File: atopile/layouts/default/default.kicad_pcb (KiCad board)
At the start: 2 copper layers, 78 x 60 mm, 86 parts

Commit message: Add schematic PDF export and name remaining nets
- scripts/export_schematic.py: builds a hierarchical KiCad schematic
  from atopile's outputs (PCB netlist, BOM values, per-part symbols),
  one sheet per subsystem with a net label on every pin, plots it with
  kicad-cli and verifies the schematic netlist matches the atopile
  netlist net-for-net
- schematic/: generated KiCad 10 schematic + solartron_7075_usb.pdf
- Name previously auto-named nets in the .ato source (XIN, XTAL_OUT,
  VREG_AVDD, BOOTSEL_SW, LDO_FB, STATUS_LED, LED anodes, shift-register
  chain links, SAMPLE_CONTACT_GATE)
- README: schematic section and converter circle-syntax note

Co-Authored-By: Claude Opus 5.5 <noreply@anthropic.com>
Claude-Session: https://claude.ai/code/session_01NqBEt2iCuw3VMJkgzgPtpr
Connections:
- net 37 renamed STATUS_LED
- net DS renamed SI_CHAIN_1
- net G renamed SAMPLE_CONTACT_GATE
- net anode renamed LED_ISO_A
- net anode-1 renamed LED_PWR_A
- net anode-2 renamed LED_STATUS_A
- net crystal_load[0]-power-hv renamed XIN
- net crystal_load[1]-power-hv renamed XTAL_OUT
- net hv renamed LDO_FB
- net input renamed BOOTSEL_SW
- net serial_in-DS renamed SO_CHAIN_1
- net shift_in[2]-q7-DS renamed SI_CHAIN_2
- net shift_in[3]-q7-DS renamed SI_CHAIN_3
- net shift_in[4]-q7-DS renamed SI_CHAIN_4
- net vreg_avdd_c-power-hv renamed VREG_AVDD
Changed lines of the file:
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@@
 	(net 30 "SKB50_RANGE_CMD_4")
 	(net 31 "SKB09_D4_1")
-	(net 32 "anode")
-	(net 33 "hv")
+	(net 32 "LED_ISO_A")
+	(net 33 "LDO_FB")
 	(net 34 "DNC")
-	(net 35 "input")
+	(net 35 "BOOTSEL_SW")
 	(net 36 "QSPI_SS")
-	(net 37 "crystal_load[0]-power-hv")
-	(net 38 "crystal_load[1]-power-hv")
+	(net 37 "XIN")
+	(net 38 "XTAL_OUT")
 	(net 39 "GND")
 	(net 40 "10")
@@
 	(net 56 "35")
 	(net 57 "36")
-	(net 58 "37")
+	(net 58 "STATUS_LED")
 	(net 59 "+1V1")
 	(net 60 "4")
@@
 	(net 63 "42")
 	(net 64 "43")
-	(net 65 "vreg_avdd_c-power-hv")
+	(net 65 "VREG_AVDD")
 	(net 66 "VREG_LX")
 	(net 67 "5")
@@
 	(net 93 "opto_sck-AN")
 	(net 94 "SCK")
-	(net 95 "anode-1")
-	(net 96 "DS")
+	(net 95 "LED_PWR_A")
+	(net 96 "SI_CHAIN_1")
 	(net 97 "SKB08_D4_2")
 	(net 98 "SKB07_D4_4")
@@
 	(net 108 "SKB13_D3_1")
 	(net 109 "shift_in[1]-q7_n-7")
-	(net 110 "shift_in[3]-q7-DS")
+	(net 110 "SI_CHAIN_3")
 	(net 111 "SKB23_D0_4")
 	(net 112 "SKB22_D0_8")
@@
 	(net 114 "SKB20_D1_2")
 	(net 115 "shift_in[2]-q7_n-7")
-	(net 116 "shift_in[2]-q7-DS")
+	(net 116 "SI_CHAIN_2")
 	(net 117 "SKB29_FUNC_OUT_B")
 	(net 118 "SKB28_FUNC_OUT_A")
@@
 	(net 123 "SKB35_DATA_CAN_CHANGE")
 	(net 124 "shift_in[4]-q7_n-7")
-	(net 125 "shift_in[4]-q7-DS")
-	(net 126 "G")
+	(net 125 "SI_CHAIN_4")
+	(net 126 "SAMPLE_CONTACT_GATE")
 	(net 127 "OE_N_ISO")
 	(net 128 "MOSI_ISO")
-	(net 129 "serial_in-DS")
+	(net 129 "SO_CHAIN_1")
 	(net 130 "q[5]-5")
 	(net 131 "6")
 	(net 132 "q[7]-7")
 	(net 133 "Q7S")
-	(net 134 "anode-2")
+	(net 134 "LED_STATUS_A")
 	(net 135 "SWO")
 	(net 136 "DATA_P")
@@
 			(size 0.36 0.61)
 			(layers "F.Cu" "F.Paste" "F.Mask")
-			(net 33 "hv")
+			(net 33 "LDO_FB")
 		)
 		(pad "3" smd oval
@@
 			(size 0.2 0.88)
 			(layers "F.Cu" "F.Paste" "F.Mask")
-			(net 65 "vreg_avdd_c-power-hv")
+			(net 65 "VREG_AVDD")
 		)
 		(pad "45" smd rect
@@
 			(size 0.88 0.2)
 			(layers "F.Cu" "F.Paste" "F.Mask")
-			(net 58 "37")
+			(net 58 "STATUS_LED")
 		)
 		(pad "36" smd rect
@@
 			(size 0.2 0.88)
 			(layers "F.Cu" "F.Paste" "F.Mask")
-			(net 37 "crystal_load[0]-power-hv")
+			(net 37 "XIN")
 		)
 		(pad "20" smd rect
@@
 			(size 1.4 1.2)
 			(layers "F.Cu" "F.Paste" "F.Mask")
-			(net 37 "crystal_load[0]-power-hv")
+			(net 37 "XIN")
 		)
 		(pad "2" smd rect
@@
 			(size 1.4 1.2)
 			(layers "F.Cu" "F.Paste" "F.Mask")
-			(net 38 "crystal_load[1]-power-hv")
+			(net 38 "XTAL_OUT")
 		)
 		(pad "4" smd rect
@@
 			(size 1.05 0.7)
 			(layers "F.Cu" "F.Paste" "F.Mask")
-			(net 35 "input")
+			(net 35 "BOOTSEL_SW")
 		)
 		(pad "2" smd rect
@@
 			(size 1.05 0.7)
 			(layers "F.Cu" "F.Paste" "F.Mask")
-			(net 35 "input")
+			(net 35 "BOOTSEL_SW")
 		)
 		(pad "3" smd rect
@@
 			(size 0.8 0.8)
 			(layers "F.Cu" "F.Paste" "F.Mask")
-			(net 95 "anode-1")
+			(net 95 "LED_PWR_A")
 		)
 		(pad "1" smd rect
@@
 			(size 0.8 0.8)
 			(layers "F.Cu" "F.Paste" "F.Mask")
-			(net 134 "anode-2")
+			(net 134 "LED_STATUS_A")
 		)
 		(pad "2" smd rect
@@
 			(size 0.8 0.8)
 			(layers "F.Cu" "F.Paste" "F.Mask")
-			(net 32 "anode")
+			(net 32 "LED_ISO_A")
 		)
 		(pad "1" smd rect
@@
 			(size 0.6 1.97)
 			(layers "F.Cu" "F.Paste" "F.Mask")
-			(net 96 "DS")
+			(net 96 "SI_CHAIN_1")
 		)
 		(pad "9" smd oval
@@
 			(size 0.6 1.97)
 			(layers "F.Cu" "F.Paste" "F.Mask")
-			(net 116 "shift_in[2]-q7-DS")
+			(net 116 "SI_CHAIN_2")
 		)
 		(pad "9" smd oval
@@
 			(size 0.6 1.97)
 			(layers "F.Cu" "F.Paste" "F.Mask")
-			(net 96 "DS")
+			(net 96 "SI_CHAIN_1")
 		)
 		(embedded_fonts no)
@@
 			(size 0.6 1.97)
 			(layers "F.Cu" "F.Paste" "F.Mask")
-			(net 110 "shift_in[3]-q7-DS")
+			(net 110 "SI_CHAIN_3")
 		)
 		(pad "9" smd oval
@@
 			(size 0.6 1.97)
 			(layers "F.Cu" "F.Paste" "F.Mask")
-			(net 116 "shift_in[2]-q7-DS")
+			(net 116 "SI_CHAIN_2")
 		)
 		(embedded_fonts no)
@@
 			(size 0.6 1.97)
 			(layers "F.Cu" "F.Paste" "F.Mask")
-			(net 125 "shift_in[4]-q7-DS")
+			(net 125 "SI_CHAIN_4")
 		)
 		(pad "9" smd oval
@@
 			(size 0.6 1.97)
 			(layers "F.Cu" "F.Paste" "F.Mask")
-			(net 110 "shift_in[3]-q7-DS")
+			(net 110 "SI_CHAIN_3")
 		)
 		(embedded_fonts no)
@@
 			(size 0.6 1.97)
 			(layers "F.Cu" "F.Paste" "F.Mask")
-			(net 125 "shift_in[4]-q7-DS")
+			(net 125 "SI_CHAIN_4")
 		)
 		(embedded_fonts no)
@@
 			(size 0.6 1.97)
 			(layers "F.Cu" "F.Paste" "F.Mask")
-			(net 126 "G")
+			(net 126 "SAMPLE_CONTACT_GATE")
 		)
 		(pad "2" smd oval
@@
 			(size 0.6 1.97)
 			(layers "F.Cu" "F.Paste" "F.Mask")
-			(net 129 "serial_in-DS")
+			(net 129 "SO_CHAIN_1")
 		)
 		(embedded_fonts no)
@@
 			(size 0.6 1.97)
 			(layers "F.Cu" "F.Paste" "F.Mask")
-			(net 129 "serial_in-DS")
+			(net 129 "SO_CHAIN_1")
 		)
 		(pad "13" smd oval
@@
 			(size 1 0.65)
 			(layers "F.Cu" "F.Paste" "F.Mask")
-			(net 126 "G")
+			(net 126 "SAMPLE_CONTACT_GATE")
 		)
 		(pad "2" smd rect
@@
 			(size 0.57 0.54)
 			(layers "F.Cu" "F.Paste" "F.Mask")
-			(net 32 "anode")
+			(net 32 "LED_ISO_A")
 		)
 		(pad "1" smd rect
@@
 			(size 0.57 0.54)
 			(layers "F.Cu" "F.Paste" "F.Mask")
-			(net 33 "hv")
+			(net 33 "LDO_FB")
 		)
 		(pad "1" smd rect
@@
 			(size 0.57 0.54)
 			(layers "F.Cu" "F.Paste" "F.Mask")
-			(net 126 "G")
+			(net 126 "SAMPLE_CONTACT_GATE")
 		)
 		(embedded_fonts no)
@@
 			(size 0.57 0.54)
 			(layers "F.Cu" "F.Paste" "F.Mask")
-			(net 33 "hv")
+			(net 33 "LDO_FB")
 		)
 		(embedded_fonts no)
@@
 			(size 0.57 0.54)
 			(layers "F.Cu" "F.Paste" "F.Mask")
-			(net 35 "input")
+			(net 35 "BOOTSEL_SW")
 		)
 		(pad "1" smd rect
@@
 			(size 0.57 0.54)
 			(layers "F.Cu" "F.Paste" "F.Mask")
-			(net 38 "crystal_load[1]-power-hv")
+			(net 38 "XTAL_OUT")
 		)
 		(pad "1" smd rect
@@
 			(size 0.5 0.54)
 			(layers "F.Cu" "F.Paste" "F.Mask")
-			(net 37 "crystal_load[0]-power-hv")
+			(net 37 "XIN")
 		)
 		(embedded_fonts no)
@@
 			(size 0.5 0.54)
 			(layers "F.Cu" "F.Paste" "F.Mask")
-			(net 38 "crystal_load[1]-power-hv")
+			(net 38 "XTAL_OUT")
 		)
 		(embedded_fonts no)
@@
 			(size 0.5 0.54)
 			(layers "F.Cu" "F.Paste" "F.Mask")
-			(net 65 "vreg_avdd_c-power-hv")
+			(net 65 "VREG_AVDD")
 		)
 		(embedded_fonts no)
@@
 			(size 0.57 0.54)
 			(layers "F.Cu" "F.Paste" "F.Mask")
-			(net 65 "vreg_avdd_c-power-hv")
+			(net 65 "VREG_AVDD")
 		)
 		(pad "1" smd rect
@@
 			(size 0.57 0.54)
 			(layers "F.Cu" "F.Paste" "F.Mask")
-			(net 95 "anode-1")
+			(net 95 "LED_PWR_A")
 		)
 		(pad "1" smd rect
@@
 			(size 0.57 0.54)
 			(layers "F.Cu" "F.Paste" "F.Mask")
-			(net 134 "anode-2")
+			(net 134 "LED_STATUS_A")
 		)
 		(pad "1" smd rect
@@
 			(size 0.57 0.54)
 			(layers "F.Cu" "F.Paste" "F.Mask")
-			(net 58 "37")
+			(net 58 "STATUS_LED")
 		)
 		(embedded_fonts no)

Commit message: atopile: gerbers, 1:1 prints and 3D renders of the PCB
- scripts/export_pcb.py: DRC with zone refill, gerbers + Excellon drill
  (zipped, named _UNROUTED_ while DRC reports unrouted connections),
  3-page 1:1 A4 prints with title block, and 3D renders, all from a
  temporary copy of the atopile layout
- layouts/default/default.kicad_pro: JLCPCB 2-layer design rules
- place_components.py: move the pre-routed TLV75901 block (parts,
  tracks, vias) rigidly; pours to the barrier edge; DC-DC and R10 moved
  clear of the board edge; zone polygons without uuid (KiCad 10)
- check_layout.py: pad-to-pad check inside pre-routed library blocks
- Fix EasyEDA 3D model offsets for IB0505LS (y), USB-B (z) and DD-50 (z)
- README: PCB outputs section, DRC status, stack-up and tool notes

The board is still unrouted; the gerbers are for fit checks only.

Co-Authored-By: Claude Opus 5.5 <noreply@anthropic.com>
Claude-Session: https://claude.ai/code/session_01NqBEt2iCuw3VMJkgzgPtpr
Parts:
- moved C4 4.64 mm to (-10.3, -23.2), turned to 180 degrees
- moved R3 4.54 mm to (-13.8, -23.2)
- moved C5 4.46 mm to (-13.5, -26.7), turned to 0 degrees
- moved R2 3.17 mm to (-14.2, -25.0), turned to -90 degrees
- moved R10 1.90 mm to (-29.6, 3.80)
- moved U2 0.60 mm to (-33.4, 1.27)

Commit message: atopile: pin-swap the shift registers to untangle the DD-50 routing
- scripts/pin_swap.py: treats all 74HCT165 inputs, all 74HCT595 outputs
  and both chain orders as interchangeable, minimises ratsnest length +
  crossings (seeded simulated annealing) and regenerates the pin-map
  block in main.ato and the firmware bit-map tables in README.md
- DVM-side ratsnest: 1544 mm / 839 crossings -> 860 mm / 154 crossings;
  165 chain now follows the physical row (124 mm -> 56 mm)
- place_components.py: fixed register slots (the old centroid sort was
  not idempotent once the DD-50 sat on B.Cu and reversed the row)
- schematic, ERC and fab outputs regenerated; no parts moved

Co-Authored-By: Claude Opus 5.5 <noreply@anthropic.com>
Claude-Session: https://claude.ai/code/session_01NqBEt2iCuw3VMJkgzgPtpr
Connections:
- U12 pad 11: SKB08_D4_2 -> +5V_ISO
- U12 pad 12: SKB07_D4_4 -> +5V_ISO
- U12 pad 13: SKB06_D4_8 -> SKB32_RANGE_OUT_1
- U12 pad 14: SKB05_D5_1 -> SKB15_D2_4
- U12 pad 3: SKB04_D5_2 -> SKB17_D2_1
- U12 pad 4: SKB03_D5_4 -> SKB16_D2_2
- U12 pad 5: SKB02_D5_8 -> SKB33_PRINT_PULSE
- U12 pad 6: SKB01_D6_1 -> GND_ISO
- U13 pad 10: SI_CHAIN_2 -> GND_ISO
- U13 pad 11: SKB16_D2_2 -> SKB34_PRINT_LEVEL
- U13 pad 12: SKB15_D2_4 -> SKB01_D6_1
- U13 pad 13: SKB14_D2_8 -> SKB35_DATA_CAN_CHANGE
- U13 pad 14: SKB13_D3_1 -> SKB18_D1_8
- U13 pad 3: SKB12_D3_2 -> SKB03_D5_4
- U13 pad 4: SKB11_D3_4 -> SKB36_OVERLOAD
- U13 pad 5: SKB10_D3_8 -> SKB19_D1_4
- U13 pad 6: SKB09_D4_1 -> SKB02_D5_8
- U13 pad 9: SI_CHAIN_1 -> SI_CHAIN_4
- U14 pad 12: SKB23_D0_4 -> SKB25_D0_1
- U14 pad 13: SKB22_D0_8 -> SKB08_D4_2
- U14 pad 14: SKB21_D1_1 -> SKB26_POL_POS
- U14 pad 3: SKB20_D1_2 -> SKB28_FUNC_OUT_A
- U14 pad 4: SKB19_D1_4 -> SKB10_D3_8
- U14 pad 5: SKB18_D1_8 -> SKB27_POL_NEG
- U14 pad 6: SKB17_D2_1 -> SKB09_D4_1
- U15 pad 11: SKB32_RANGE_OUT_1 -> SKB20_D1_2
- U15 pad 12: SKB31_RANGE_OUT_2 -> SKB04_D5_2
- U15 pad 13: SKB30_RANGE_OUT_4 -> SKB21_D1_1
- U15 pad 14: SKB29_FUNC_OUT_B -> SKB05_D5_1
- U15 pad 3: SKB28_FUNC_OUT_A -> SKB07_D4_4
- U15 pad 4: SKB27_POL_NEG -> SKB23_D0_4
- U15 pad 5: SKB26_POL_POS -> SKB06_D4_8
- U15 pad 6: SKB25_D0_1 -> SKB22_D0_8
- U16 pad 10: GND_ISO -> SI_CHAIN_2
- U16 pad 11: GND_ISO -> SKB11_D3_4
- U16 pad 12: +5V_ISO -> GND_ISO
- U16 pad 13: GND_ISO -> SKB29_FUNC_OUT_B
- U16 pad 14: +5V_ISO -> SKB12_D3_2
- U16 pad 3: SKB36_OVERLOAD -> SKB14_D2_8
- U16 pad 4: SKB35_DATA_CAN_CHANGE -> SKB31_RANGE_OUT_2
- U16 pad 5: SKB34_PRINT_LEVEL -> SKB13_D3_1
- U16 pad 6: SKB33_PRINT_PULSE -> SKB30_RANGE_OUT_4
- U16 pad 9: SI_CHAIN_4 -> SI_CHAIN_1
- U17 pad 1: SAMPLE_CONTACT_GATE -> SKB44_INT_TIME_4
- U17 pad 14: MOSI_ISO -> SO_CHAIN_1
- U17 pad 15: SKB38_LOCKOUT -> SKB43_FUNC_CMD_B
- U17 pad 2: SKB40_SAMPLE_PULSE -> SKB45_INT_TIME_2
- U17 pad 3: SKB41_RATIO -> SKB46_INT_TIME_1
- U17 pad 4: SKB42_FUNC_CMD_A -> SKB47_AUTORANGE
- U17 pad 5: SKB43_FUNC_CMD_B -> SKB48_RANGE_CMD_1
- U17 pad 6: SKB44_INT_TIME_4 -> SKB49_RANGE_CMD_2
- U17 pad 7: SKB45_INT_TIME_2 -> SKB50_RANGE_CMD_4
- U17 pad 9: SO_CHAIN_1 -> Q7S
- U18 pad 1: SKB47_AUTORANGE -> SKB38_LOCKOUT
- U18 pad 14: SO_CHAIN_1 -> MOSI_ISO
- U18 pad 15: SKB46_INT_TIME_1 -> q[0]-15
- U18 pad 2: SKB48_RANGE_CMD_1 -> q[2]-2
- U18 pad 3: SKB49_RANGE_CMD_2 -> q[3]-3
- U18 pad 4: SKB50_RANGE_CMD_4 -> SKB40_SAMPLE_PULSE
- U18 pad 5: q[5]-5 -> SKB41_RATIO
- U18 pad 6: 6 -> SKB42_FUNC_CMD_A
- U18 pad 7: q[7]-7 -> SAMPLE_CONTACT_GATE
- U18 pad 9: Q7S -> SO_CHAIN_1

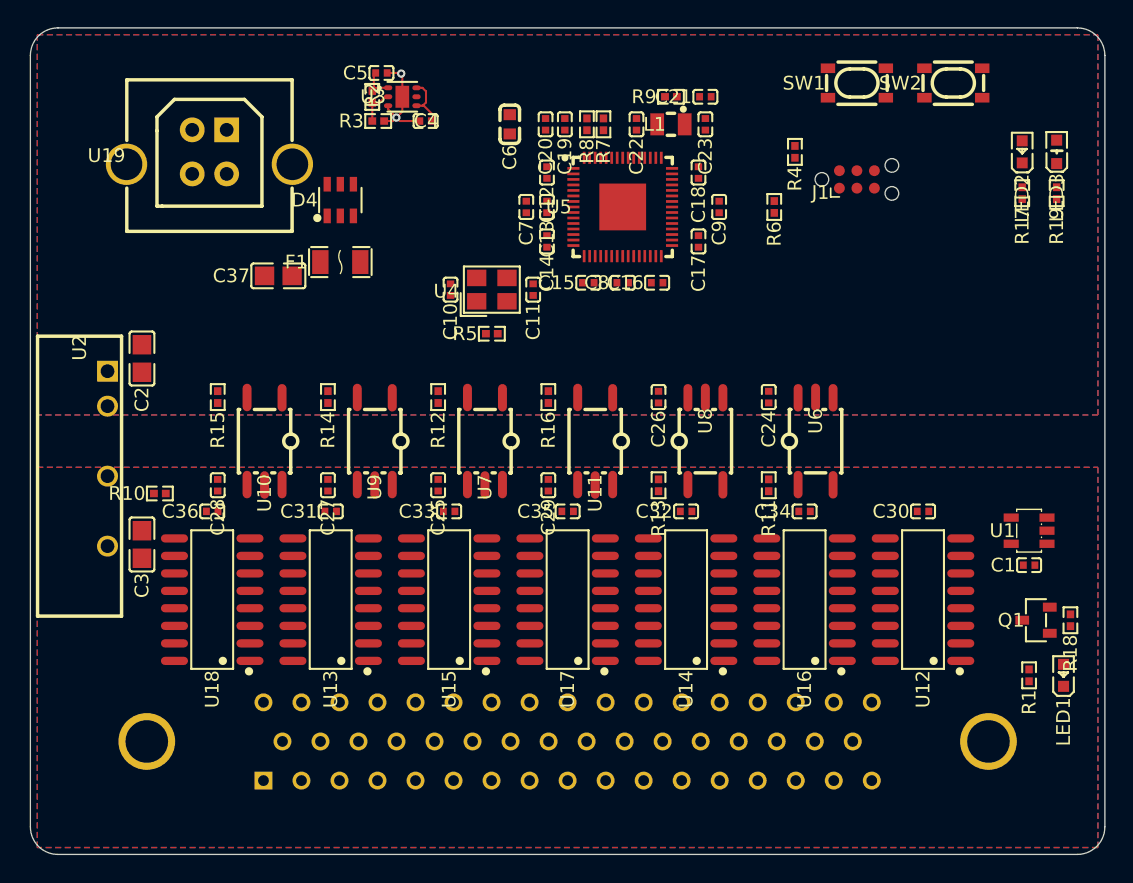
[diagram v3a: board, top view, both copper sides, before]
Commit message: atopile: move DVM-side parts for routing, then redo the pin swap
- optimise_placement.py result: IC row (E->W) 165,595,165,595,165,165,165
  with the 165s turned 180 deg; DRDY buffer to the west end next to SKB 34;
  SAMPLE MOSFET + pull-down south of the DD-50 in line with SKB 39; opto
  order W->E DRDY, MISO, LATCH, MOSI, OE_N, SCK
- pin_swap.py: control nets (SCK/LATCH/OE_N/DRDY, SKB 39 drain, MCU<->opto)
  now count for crossings; longer annealing and a chain-reversal move so
  all restarts converge
- DVM ratsnest incl. control nets: 1206 mm / 297 crossings (pin swap only)
  -> 985 mm / 112 crossings (original: 1889 mm / 1000)
- schematic, ERC, fab outputs, placement picture and README regenerated

Co-Authored-By: Claude Opus 5.5 <noreply@anthropic.com>
Claude-Session: https://claude.ai/code/session_01NqBEt2iCuw3VMJkgzgPtpr
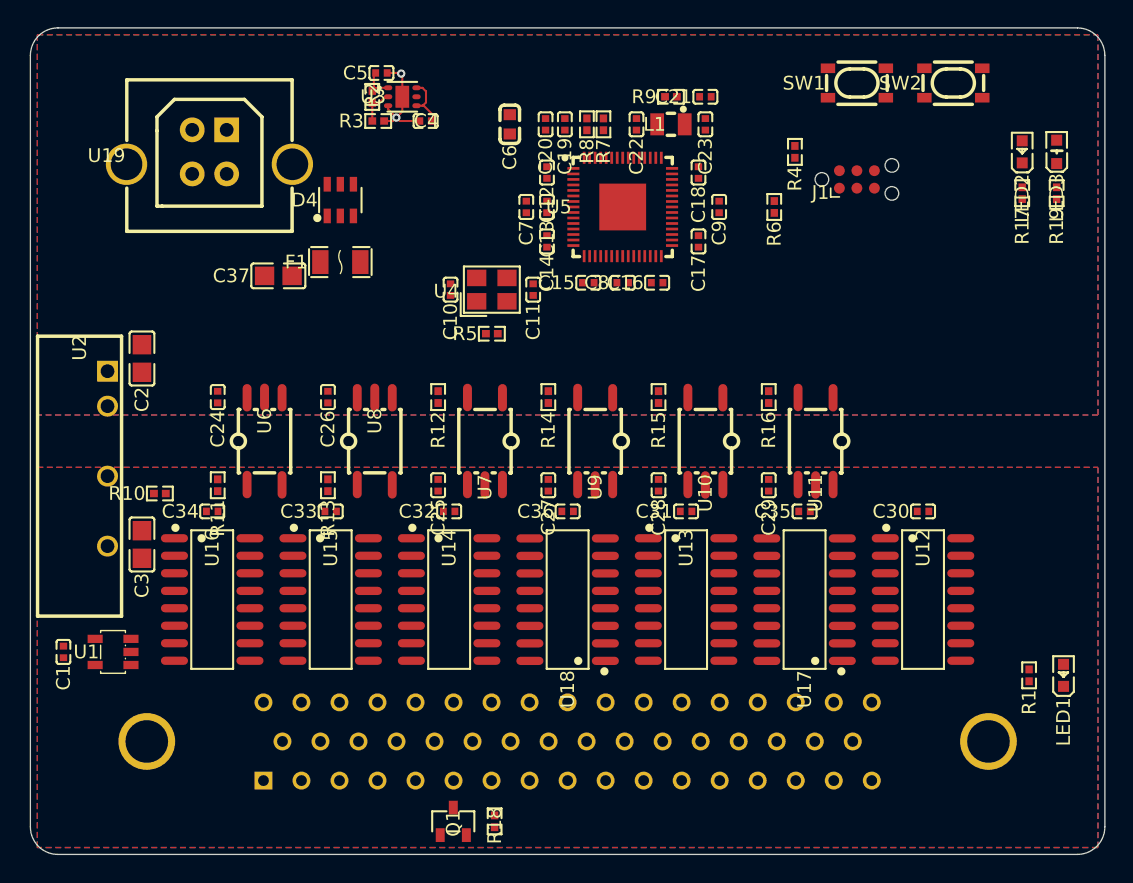
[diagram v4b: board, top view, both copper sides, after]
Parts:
- moved C1 70.4 mm to (-36.6, 15.3), turned to 90 degrees
- moved U1 67.1 mm to (-33.0, 15.3)
- moved Q1 44.7 mm to (-8.30, 27.6), turned to 270 degrees
- moved R18 44.3 mm to (-5.30, 27.6), turned to 270 degrees
- moved C34 43.0 mm to (-25.8, 5.10)
- moved U16 43.0 mm to (-25.8, 11.5), turned to 270 degrees
- moved C24 40.0 mm to (-25.4, -3.20)
- moved R11 40.0 mm to (-25.4, 3.20)
- moved U6 40.0 mm to (-22.0, 0.00)
- moved C28 32.0 mm to (6.60, 3.20)
- moved R15 32.0 mm to (6.60, -3.20)
- moved U10 32.0 mm to (10.0, 0.00)
- moved C36 25.8 mm to (0.00, 5.10)
- moved U18 25.8 mm to (0.00, 11.5)
- moved C31 25.8 mm to (8.60, 5.10)
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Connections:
- U12 pad 10: SI_CHAIN_1 -> GND_ISO
- U12 pad 11: +5V_ISO -> SKB17_D2_1
- U12 pad 12: +5V_ISO -> SKB16_D2_2
- U12 pad 13: SKB32_RANGE_OUT_1 -> SKB33_PRINT_PULSE
- U12 pad 3: SKB17_D2_1 -> SKB30_RANGE_OUT_4
- U12 pad 4: SKB16_D2_2 -> SKB31_RANGE_OUT_2
- U12 pad 5: SKB33_PRINT_PULSE -> SKB14_D2_8
- U12 pad 6: GND_ISO -> SKB32_RANGE_OUT_1
- U12 pad 9: MISO_ISO -> SI_CHAIN_4
- U13 pad 10: GND_ISO -> SI_CHAIN_4
- U13 pad 11: SKB34_PRINT_LEVEL -> SKB13_D3_1
- U13 pad 12: SKB01_D6_1 -> SKB29_FUNC_OUT_B
- U13 pad 13: SKB35_DATA_CAN_CHANGE -> SKB12_D3_2
- U13 pad 14: SKB18_D1_8 -> SKB28_FUNC_OUT_A
- U13 pad 3: SKB03_D5_4 -> SKB26_POL_POS
- U13 pad 4: SKB36_OVERLOAD -> SKB10_D3_8
- U13 pad 5: SKB19_D1_4 -> SKB27_POL_NEG
- U13 pad 6: SKB02_D5_8 -> SKB11_D3_4
- U13 pad 9: SI_CHAIN_4 -> SI_CHAIN_3
- U14 pad 11: SKB24_D0_2 -> SKB08_D4_2
- U14 pad 13: SKB08_D4_2 -> SKB09_D4_1
- U14 pad 14: SKB26_POL_POS -> +5V_ISO
- U14 pad 3: SKB28_FUNC_OUT_A -> SKB24_D0_2
- U14 pad 4: SKB10_D3_8 -> SKB07_D4_4
- U14 pad 5: SKB27_POL_NEG -> SKB23_D0_4
- U14 pad 6: SKB09_D4_1 -> SKB06_D4_8
- U15 pad 10: SI_CHAIN_4 -> SI_CHAIN_2
- U15 pad 11: SKB20_D1_2 -> SKB04_D5_2
- U15 pad 12: SKB04_D5_2 -> SKB21_D1_1
- U15 pad 13: SKB21_D1_1 -> SKB05_D5_1
- U15 pad 14: SKB05_D5_1 -> SKB22_D0_8
- U15 pad 3: SKB07_D4_4 -> SKB20_D1_2
- U15 pad 4: SKB23_D0_4 -> SKB36_OVERLOAD
- U15 pad 5: SKB06_D4_8 -> SKB03_D5_4
- U15 pad 6: SKB22_D0_8 -> SKB19_D1_4
- U15 pad 9: SI_CHAIN_3 -> SI_CHAIN_1
- U16 pad 10: SI_CHAIN_2 -> SI_CHAIN_1
- U16 pad 11: SKB11_D3_4 -> SKB35_DATA_CAN_CHANGE
- U16 pad 13: SKB29_FUNC_OUT_B -> +5V_ISO
- U16 pad 14: SKB12_D3_2 -> GND_ISO
- U16 pad 3: SKB14_D2_8 -> SKB18_D1_8
- U16 pad 4: SKB31_RANGE_OUT_2 -> SKB02_D5_8
- U16 pad 5: SKB13_D3_1 -> SKB34_PRINT_LEVEL
- U16 pad 6: SKB30_RANGE_OUT_4 -> SKB01_D6_1
- U16 pad 9: SI_CHAIN_1 -> MISO_ISO
- U17 pad 1: SKB44_INT_TIME_4 -> SKB49_RANGE_CMD_2
- U17 pad 15: SKB43_FUNC_CMD_B -> SKB45_INT_TIME_2
- U17 pad 2: SKB45_INT_TIME_2 -> SKB50_RANGE_CMD_4
- U17 pad 3: SKB46_INT_TIME_1 -> SKB48_RANGE_CMD_1
- U17 pad 5: SKB48_RANGE_CMD_1 -> SKB46_INT_TIME_1
- U17 pad 6: SKB49_RANGE_CMD_2 -> 6
- U17 pad 7: SKB50_RANGE_CMD_4 -> shift_out[0]-q[7]-7
- U18 pad 1: SKB38_LOCKOUT -> SAMPLE_CONTACT_GATE
- U18 pad 15: q[0]-15 -> SKB38_LOCKOUT
- U18 pad 2: q[2]-2 -> SKB43_FUNC_CMD_B
- U18 pad 3: q[3]-3 -> SKB42_FUNC_CMD_A
- U18 pad 4: SKB40_SAMPLE_PULSE -> SKB44_INT_TIME_4
- U18 pad 6: SKB42_FUNC_CMD_A -> SKB40_SAMPLE_PULSE
- U18 pad 7: SAMPLE_CONTACT_GATE -> shift_out[1]-q[7]-7
